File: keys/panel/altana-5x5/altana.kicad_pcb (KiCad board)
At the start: 2 copper layers, 94 x 94 mm, 75 parts, among them SW1 SW_PUSH, SW10 SW_PUSH, SW11 SW_PUSH, SW12 SW_PUSH, SW13 SW_PUSH, SW14 SW_PUSH, SW15 SW_PUSH, SW16 SW_PUSH, SW17 SW_PUSH, SW18 SW_PUSH, SW19 SW_PUSH, SW2 SW_PUSH, SW20 SW_PUSH, SW21 SW_PUSH, SW22 SW_PUSH, SW23 SW_PUSH, SW24 SW_PUSH, SW25 SW_PUSH, SW3 SW_PUSH, SW4 SW_PUSH, SW5 SW_PUSH, SW6 SW_PUSH, SW7 SW_PUSH, SW8 SW_PUSH, SW9 SW_PUSH

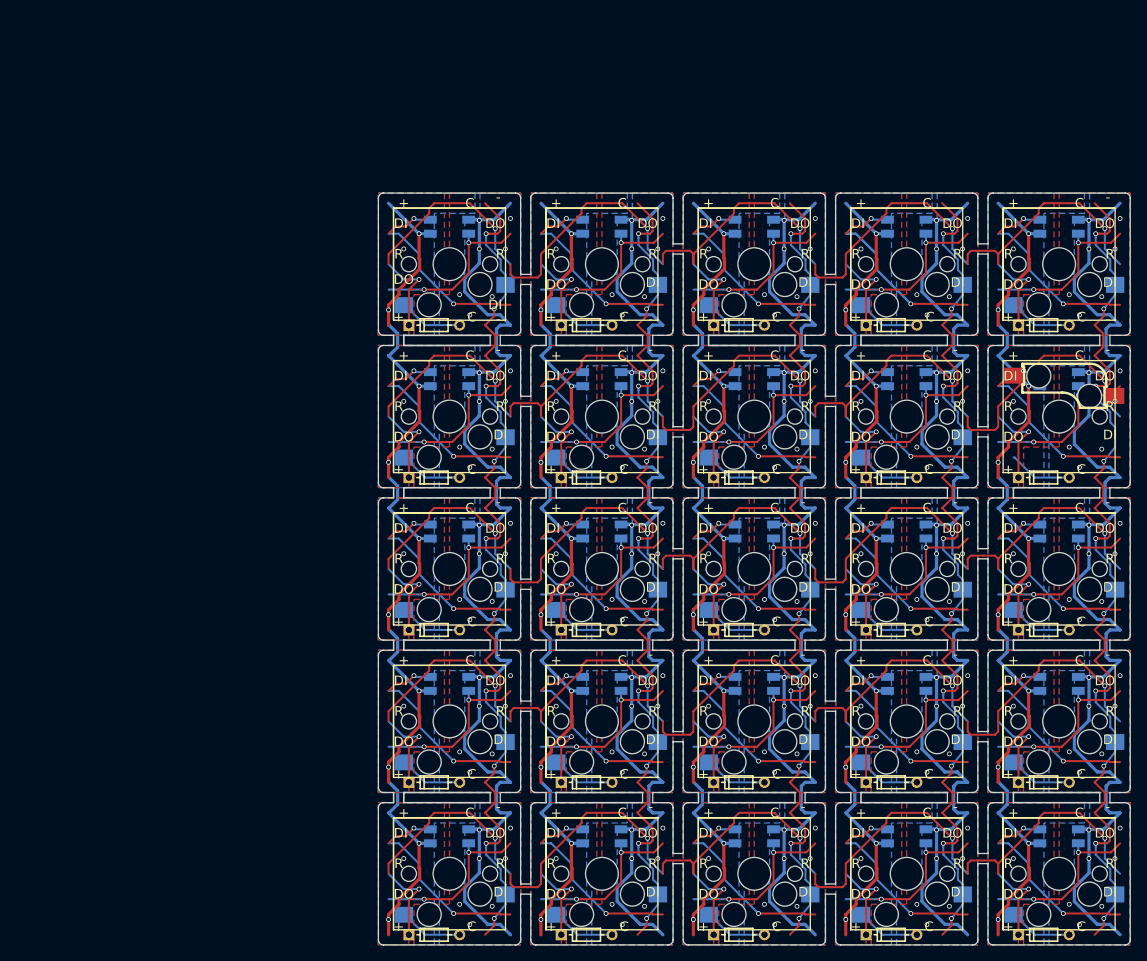
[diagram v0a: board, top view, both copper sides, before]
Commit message: Restore original panel
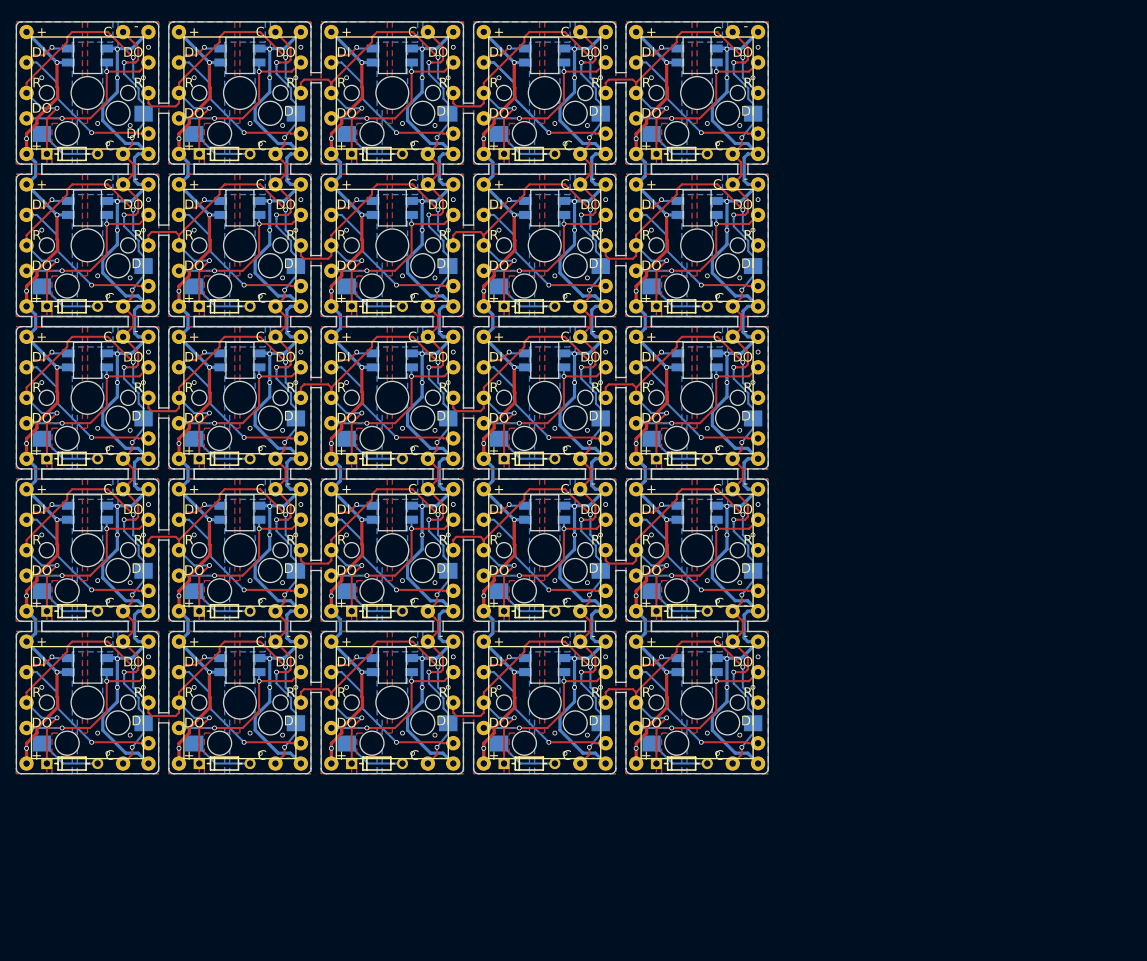
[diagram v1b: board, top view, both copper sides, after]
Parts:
- added REF**: wire pad, footprint:wirepad, B.Cu at (120.1, 54.7)
- added REF**: wire pad, footprint:wirepad, B.Cu at (143.0, 111.9)
- added REF**: wire pad, footprint:wirepad, B.Cu at (158.2, 108.1)
- added REF**: wire pad, footprint:wirepad, B.Cu at (139.2, 108.1)
- added REF**: wire pad, footprint:wirepad, B.Cu at (120.1, 108.1)
- added REF**: wire pad, footprint:wirepad, B.Cu at (101.1, 108.1)
- added REF**: wire pad, footprint:wirepad, B.Cu at (82.0, 108.1)
- added REF**: wire pad, footprint:wirepad, B.Cu at (158.2, 89.0)
- added REF**: wire pad, footprint:wirepad, B.Cu at (139.2, 89.0)
- added REF**: wire pad, footprint:wirepad, B.Cu at (120.1, 89.0)
- added REF**: wire pad, footprint:wirepad, B.Cu at (101.1, 89.0)
- added REF**: wire pad, footprint:wirepad, B.Cu at (82.0, 89.0)
- added REF**: wire pad, footprint:wirepad, B.Cu at (124.0, 111.9)
- added REF**: wire pad, footprint:wirepad, B.Cu at (158.2, 70.0)
- added REF**: wire pad, footprint:wirepad, B.Cu at (139.2, 70.0)
- added REF**: wire pad, footprint:wirepad, B.Cu at (120.1, 70.0)
- added REF**: wire pad, footprint:wirepad, B.Cu at (101.1, 70.0)
- added REF**: wire pad, footprint:wirepad, B.Cu at (82.0, 70.0)
- added REF**: wire pad, footprint:wirepad, B.Cu at (158.2, 50.9)
- added REF**: wire pad, footprint:wirepad, B.Cu at (139.2, 50.9)
- added REF**: wire pad, footprint:wirepad, B.Cu at (120.1, 50.9)
- added REF**: wire pad, footprint:wirepad, B.Cu at (101.1, 50.9)
- added REF**: wire pad, footprint:wirepad, B.Cu at (82.0, 50.9)
- added REF**: wire pad, footprint:wirepad, B.Cu at (104.9, 111.9)
- added REF**: wire pad, footprint:wirepad, B.Cu at (158.2, 31.9)
- added REF**: wire pad, footprint:wirepad, B.Cu at (139.2, 31.9)
- added REF**: wire pad, footprint:wirepad, B.Cu at (120.1, 31.9)
- added REF**: wire pad, footprint:wirepad, B.Cu at (101.1, 31.9)
- added REF**: wire pad, footprint:wirepad, B.Cu at (155.1, 100.5)
- added REF**: wire pad, footprint:wirepad, B.Cu at (143.0, 119.5)
- added REF**: wire pad, footprint:wirepad, B.Cu at (143.0, 104.3)
- added REF**: wire pad, footprint:wirepad, B.Cu at (158.2, 104.3)
- added REF**: wire pad, footprint:wirepad, B.Cu at (155.1, 104.3)
- added REF**: wire pad, footprint:wirepad, B.Cu at (158.2, 119.5)
- added REF**: wire pad, footprint:wirepad, B.Cu at (85.9, 111.9)
- added REF**: wire pad, footprint:wirepad, B.Cu at (155.1, 119.5)
- added REF**: wire pad, footprint:wirepad, B.Cu at (124.0, 119.5)
- added REF**: wire pad, footprint:wirepad, B.Cu at (139.2, 119.5)
- added REF**: wire pad, footprint:wirepad, B.Cu at (136.0, 104.3)
- added REF**: wire pad, footprint:wirepad, B.Cu at (139.2, 104.3)
- added REF**: wire pad, footprint:wirepad, B.Cu at (136.0, 119.5)
- added REF**: wire pad, footprint:wirepad, B.Cu at (124.0, 104.3)
- added REF**: wire pad, footprint:wirepad, B.Cu at (104.9, 104.3)
- added REF**: wire pad, footprint:wirepad, B.Cu at (104.9, 119.5)
- added REF**: wire pad, footprint:wirepad, B.Cu at (120.1, 104.3)
- added REF**: wire pad, footprint:wirepad, B.Cu at (158.2, 92.8)
- added REF**: wire pad, footprint:wirepad, B.Cu at (120.1, 119.5)
- added REF**: wire pad, footprint:wirepad, B.Cu at (117.0, 119.5)
- added REF**: wire pad, footprint:wirepad, B.Cu at (117.0, 104.3)
- added REF**: wire pad, footprint:wirepad, B.Cu at (97.9, 119.5)
- added REF**: wire pad, footprint:wirepad, B.Cu at (101.1, 119.5)
- added REF**: wire pad, footprint:wirepad, B.Cu at (85.9, 104.3)
- added REF**: wire pad, footprint:wirepad, B.Cu at (85.9, 119.5)
- added REF**: wire pad, footprint:wirepad, B.Cu at (101.1, 104.3)
- added REF**: wire pad, footprint:wirepad, B.Cu at (97.9, 104.3)
- added REF**: wire pad, footprint:wirepad, B.Cu at (82.0, 119.5)
- added REF**: wire pad, footprint:wirepad, B.Cu at (139.2, 92.8)
- added REF**: wire pad, footprint:wirepad, B.Cu at (78.9, 119.5)
- added REF**: wire pad, footprint:wirepad, B.Cu at (78.9, 104.3)
- added REF**: wire pad, footprint:wirepad, B.Cu at (66.8, 119.5)
- added REF**: wire pad, footprint:wirepad, B.Cu at (66.8, 104.3)
- added REF**: wire pad, footprint:wirepad, B.Cu at (82.0, 111.9)
- added REF**: wire pad, footprint:wirepad, B.Cu at (66.8, 111.9)
- added REF**: wire pad, footprint:wirepad, B.Cu at (82.0, 104.3)
- added REF**: wire pad, footprint:wirepad, B.Cu at (82.0, 100.5)
- added REF**: wire pad, footprint:wirepad, B.Cu at (66.8, 92.8)
- added REF**: wire pad, footprint:wirepad, B.Cu at (78.9, 85.2)
- added REF**: wire pad, footprint:wirepad, B.Cu at (120.1, 92.8)
- added REF**: wire pad, footprint:wirepad, B.Cu at (82.0, 85.2)
- added REF**: wire pad, footprint:wirepad, B.Cu at (82.0, 92.8)
- added REF**: wire pad, footprint:wirepad, B.Cu at (78.9, 100.5)
- added REF**: wire pad, footprint:wirepad, B.Cu at (66.8, 85.2)
- added REF**: wire pad, footprint:wirepad, B.Cu at (66.8, 100.5)
- added REF**: wire pad, footprint:wirepad, B.Cu at (101.1, 85.2)
- added REF**: wire pad, footprint:wirepad, B.Cu at (85.9, 85.2)
- added REF**: wire pad, footprint:wirepad, B.Cu at (97.9, 85.2)
- added REF**: wire pad, footprint:wirepad, B.Cu at (85.9, 100.5)
- added REF**: wire pad, footprint:wirepad, B.Cu at (97.9, 100.5)
- added REF**: wire pad, footprint:wirepad, B.Cu at (101.1, 92.8)
- added REF**: wire pad, footprint:wirepad, B.Cu at (101.1, 100.5)
- added REF**: wire pad, footprint:wirepad, B.Cu at (117.0, 100.5)
- added REF**: wire pad, footprint:wirepad, B.Cu at (104.9, 85.2)
- added REF**: wire pad, footprint:wirepad, B.Cu at (104.9, 100.5)
- added REF**: wire pad, footprint:wirepad, B.Cu at (117.0, 85.2)
- added REF**: wire pad, footprint:wirepad, B.Cu at (120.1, 85.2)
- added REF**: wire pad, footprint:wirepad, B.Cu at (120.1, 100.5)
- added REF**: wire pad, footprint:wirepad, B.Cu at (124.0, 100.5)
- added REF**: wire pad, footprint:wirepad, B.Cu at (124.0, 85.2)
- added REF**: wire pad, footprint:wirepad, B.Cu at (139.2, 100.5)
- added REF**: wire pad, footprint:wirepad, B.Cu at (143.0, 92.8)
- added REF**: wire pad, footprint:wirepad, B.Cu at (136.0, 85.2)
- added REF**: wire pad, footprint:wirepad, B.Cu at (136.0, 100.5)
- added REF**: wire pad, footprint:wirepad, B.Cu at (139.2, 85.2)
- added REF**: wire pad, footprint:wirepad, B.Cu at (143.0, 100.5)
- added REF**: wire pad, footprint:wirepad, B.Cu at (143.0, 85.2)
- added REF**: wire pad, footprint:wirepad, B.Cu at (158.2, 85.2)
- added REF**: wire pad, footprint:wirepad, B.Cu at (158.2, 100.5)
- added REF**: wire pad, footprint:wirepad, B.Cu at (155.1, 85.2)
- added REF**: wire pad, footprint:wirepad, B.Cu at (155.1, 66.2)
- added REF**: wire pad, footprint:wirepad, B.Cu at (143.0, 66.2)
- added REF**: wire pad, footprint:wirepad, B.Cu at (124.0, 92.8)
- added REF**: wire pad, footprint:wirepad, B.Cu at (158.2, 66.2)
- added REF**: wire pad, footprint:wirepad, B.Cu at (158.2, 81.4)
- added REF**: wire pad, footprint:wirepad, B.Cu at (155.1, 81.4)
- added REF**: wire pad, footprint:wirepad, B.Cu at (143.0, 81.4)
- added REF**: wire pad, footprint:wirepad, B.Cu at (136.0, 81.4)
- added REF**: wire pad, footprint:wirepad, B.Cu at (139.2, 81.4)
- added REF**: wire pad, footprint:wirepad, B.Cu at (124.0, 81.4)
- added REF**: wire pad, footprint:wirepad, B.Cu at (124.0, 66.2)
- added REF**: wire pad, footprint:wirepad, B.Cu at (136.0, 66.2)
- added REF**: wire pad, footprint:wirepad, B.Cu at (139.2, 66.2)
- added REF**: wire pad, footprint:wirepad, B.Cu at (139.2, 73.8)
- added REF**: wire pad, footprint:wirepad, B.Cu at (104.9, 92.8)
- added REF**: wire pad, footprint:wirepad, B.Cu at (120.1, 81.4)
- added REF**: wire pad, footprint:wirepad, B.Cu at (104.9, 81.4)
- added REF**: wire pad, footprint:wirepad, B.Cu at (117.0, 66.2)
- added REF**: wire pad, footprint:wirepad, B.Cu at (104.9, 66.2)
- added REF**: wire pad, footprint:wirepad, B.Cu at (120.1, 66.2)
- added REF**: wire pad, footprint:wirepad, B.Cu at (117.0, 81.4)
- added REF**: wire pad, footprint:wirepad, B.Cu at (85.9, 66.2)
- added REF**: wire pad, footprint:wirepad, B.Cu at (101.1, 81.4)
- added REF**: wire pad, footprint:wirepad, B.Cu at (97.9, 66.2)
- added REF**: wire pad, footprint:wirepad, B.Cu at (97.9, 81.4)
- added REF**: wire pad, footprint:wirepad, B.Cu at (85.9, 92.8)
- added REF**: wire pad, footprint:wirepad, B.Cu at (101.1, 66.2)
- added REF**: wire pad, footprint:wirepad, B.Cu at (85.9, 81.4)
- added REF**: wire pad, footprint:wirepad, B.Cu at (66.8, 81.4)
- added REF**: wire pad, footprint:wirepad, B.Cu at (78.9, 66.2)
- added REF**: wire pad, footprint:wirepad, B.Cu at (82.0, 81.4)
- added REF**: wire pad, footprint:wirepad, B.Cu at (78.9, 81.4)
- added REF**: wire pad, footprint:wirepad, B.Cu at (82.0, 73.8)
- added REF**: wire pad, footprint:wirepad, B.Cu at (82.0, 66.2)
- added REF**: wire pad, footprint:wirepad, B.Cu at (66.8, 66.2)
- added REF**: wire pad, footprint:wirepad, B.Cu at (66.8, 73.8)
- added REF**: wire pad, footprint:wirepad, B.Cu at (143.0, 73.8)
- added REF**: wire pad, footprint:wirepad, B.Cu at (104.9, 62.4)
- added REF**: wire pad, footprint:wirepad, B.Cu at (104.9, 47.1)
- added REF**: wire pad, footprint:wirepad, B.Cu at (104.9, 54.7)
- added REF**: wire pad, footprint:wirepad, B.Cu at (117.0, 62.4)
- added REF**: wire pad, footprint:wirepad, B.Cu at (120.1, 47.1)
- added REF**: wire pad, footprint:wirepad, B.Cu at (120.1, 62.4)
- added REF**: wire pad, footprint:wirepad, B.Cu at (117.0, 47.1)
- added REF**: wire pad, footprint:wirepad, B.Cu at (136.0, 47.1)
- added REF**: wire pad, footprint:wirepad, B.Cu at (124.0, 62.4)
- added REF**: wire pad, footprint:wirepad, B.Cu at (139.2, 54.7)
- added REF**: wire pad, footprint:wirepad, B.Cu at (104.9, 73.8)
- added REF**: wire pad, footprint:wirepad, B.Cu at (139.2, 47.1)
- added REF**: wire pad, footprint:wirepad, B.Cu at (139.2, 62.4)
- added REF**: wire pad, footprint:wirepad, B.Cu at (124.0, 54.7)
- added REF**: wire pad, footprint:wirepad, B.Cu at (136.0, 62.4)
- added REF**: wire pad, footprint:wirepad, B.Cu at (124.0, 47.1)
- added REF**: wire pad, footprint:wirepad, B.Cu at (158.2, 47.1)
- added REF**: wire pad, footprint:wirepad, B.Cu at (158.2, 62.4)
- added REF**: wire pad, footprint:wirepad, B.Cu at (143.0, 54.7)
- added REF**: wire pad, footprint:wirepad, B.Cu at (155.1, 62.4)
- added REF**: wire pad, footprint:wirepad, B.Cu at (155.1, 47.1)
- added REF**: wire pad, footprint:wirepad, B.Cu at (85.9, 73.8)
- added REF**: wire pad, footprint:wirepad, B.Cu at (143.0, 47.1)
- added REF**: wire pad, footprint:wirepad, B.Cu at (143.0, 62.4)
- added REF**: wire pad, footprint:wirepad, B.Cu at (158.2, 54.7)
- added REF**: wire pad, footprint:wirepad, B.Cu at (155.1, 43.3)
- added REF**: wire pad, footprint:wirepad, B.Cu at (155.1, 28.1)
- added REF**: wire pad, footprint:wirepad, B.Cu at (158.2, 28.1)
- added REF**: wire pad, footprint:wirepad, B.Cu at (143.0, 35.7)
- added REF**: wire pad, footprint:wirepad, B.Cu at (143.0, 43.3)
- added REF**: wire pad, footprint:wirepad, B.Cu at (143.0, 28.1)
- added REF**: wire pad, footprint:wirepad, B.Cu at (158.2, 35.7)
- added REF**: wire pad, footprint:wirepad, B.Cu at (158.2, 73.8)
- added REF**: wire pad, footprint:wirepad, B.Cu at (158.2, 43.3)
- added REF**: wire pad, footprint:wirepad, B.Cu at (136.0, 28.1)
- added REF**: wire pad, footprint:wirepad, B.Cu at (139.2, 28.1)
- added REF**: wire pad, footprint:wirepad, B.Cu at (124.0, 35.7)
- added REF**: wire pad, footprint:wirepad, B.Cu at (124.0, 43.3)
- added REF**: wire pad, footprint:wirepad, B.Cu at (124.0, 28.1)
- added REF**: wire pad, footprint:wirepad, B.Cu at (139.2, 35.7)
- added REF**: wire pad, footprint:wirepad, B.Cu at (136.0, 43.3)
- added REF**: wire pad, footprint:wirepad, B.Cu at (139.2, 43.3)
- added REF**: wire pad, footprint:wirepad, B.Cu at (104.9, 35.7)
- added REF**: wire pad, footprint:wirepad, B.Cu at (120.1, 73.8)
- added REF**: wire pad, footprint:wirepad, B.Cu at (104.9, 43.3)
- added REF**: wire pad, footprint:wirepad, B.Cu at (104.9, 28.1)
- added REF**: wire pad, footprint:wirepad, B.Cu at (120.1, 35.7)
- added REF**: wire pad, footprint:wirepad, B.Cu at (117.0, 28.1)
- added REF**: wire pad, footprint:wirepad, B.Cu at (120.1, 43.3)
- added REF**: wire pad, footprint:wirepad, B.Cu at (117.0, 43.3)
- added REF**: wire pad, footprint:wirepad, B.Cu at (120.1, 28.1)
- added REF**: wire pad, footprint:wirepad, B.Cu at (101.1, 62.4)
- added REF**: wire pad, footprint:wirepad, B.Cu at (97.9, 62.4)
- added REF**: wire pad, footprint:wirepad, B.Cu at (85.9, 54.7)
- added REF**: wire pad, footprint:wirepad, B.Cu at (101.1, 73.8)
- added REF**: wire pad, footprint:wirepad, B.Cu at (85.9, 62.4)
- added REF**: wire pad, footprint:wirepad, B.Cu at (85.9, 47.1)
- added REF**: wire pad, footprint:wirepad, B.Cu at (101.1, 54.7)
- added REF**: wire pad, footprint:wirepad, B.Cu at (97.9, 47.1)
- added REF**: wire pad, footprint:wirepad, B.Cu at (101.1, 47.1)
- added REF**: wire pad, footprint:wirepad, B.Cu at (82.0, 62.4)
- added REF**: wire pad, footprint:wirepad, B.Cu at (78.9, 62.4)
- added REF**: wire pad, footprint:wirepad, B.Cu at (66.8, 54.7)
- added REF**: wire pad, footprint:wirepad, B.Cu at (78.9, 47.1)
- added REF**: wire pad, footprint:wirepad, B.Cu at (82.0, 54.7)
- added REF**: wire pad, footprint:wirepad, B.Cu at (158.2, 117.0)
- added REF**: wire pad, footprint:wirepad, B.Cu at (82.0, 47.1)
- added REF**: wire pad, footprint:wirepad, B.Cu at (66.8, 47.1)
- added REF**: wire pad, footprint:wirepad, B.Cu at (66.8, 62.4)
- added REF**: wire pad, footprint:wirepad, B.Cu at (85.9, 35.7)
- added REF**: wire pad, footprint:wirepad, B.Cu at (97.9, 28.1)
- added REF**: wire pad, footprint:wirepad, B.Cu at (85.9, 28.1)
- added REF**: wire pad, footprint:wirepad, B.Cu at (85.9, 43.3)
- added REF**: wire pad, footprint:wirepad, B.Cu at (101.1, 43.3)
- added REF**: wire pad, footprint:wirepad, B.Cu at (101.1, 28.1)
- added REF**: wire pad, footprint:wirepad, B.Cu at (101.1, 35.7)
- added REF**: wire pad, footprint:wirepad, B.Cu at (139.2, 117.0)
- added REF**: wire pad, footprint:wirepad, B.Cu at (97.9, 43.3)
- added REF**: wire pad, footprint:wirepad, B.Cu at (66.8, 38.9)
- added REF**: wire pad, footprint:wirepad, B.Cu at (66.8, 31.9)
- added REF**: wire pad, footprint:wirepad, B.Cu at (82.0, 40.8)
- added REF**: wire pad, footprint:wirepad, B.Cu at (82.0, 31.9)
- added REF**: wire pad, footprint:wirepad, B.Cu at (82.0, 35.7)
- added REF**: wire pad, footprint:wirepad, B.Cu at (66.8, 35.7)
- added REF**: wire pad, footprint:wirepad, B.Cu at (82.0, 28.1)
- added REF**: wire pad, footprint:wirepad, B.Cu at (82.0, 43.3)
- added REF**: wire pad, footprint:wirepad, B.Cu at (66.8, 43.3)
- added REF**: wire pad, footprint:wirepad, B.Cu at (124.0, 73.8)
- added REF**: wire pad, footprint:wirepad, B.Cu at (120.1, 117.0)
- added REF**: wire pad, footprint:wirepad, B.Cu at (66.8, 28.1)
- added REF**: wire pad, footprint:wirepad, B.Cu at (101.1, 117.0)
- added REF**: wire pad, footprint:wirepad, B.Cu at (82.0, 117.0)
- added REF**: wire pad, footprint:wirepad, B.Cu at (158.2, 97.9)
- added REF**: wire pad, footprint:wirepad, B.Cu at (139.2, 97.9)
- added REF**: wire pad, footprint:wirepad, B.Cu at (120.1, 97.9)
- added REF**: wire pad, footprint:wirepad, B.Cu at (101.1, 97.9)
- added REF**: wire pad, footprint:wirepad, B.Cu at (82.0, 97.9)
- added REF**: wire pad, footprint:wirepad, B.Cu at (158.2, 78.9)
- added REF**: wire pad, footprint:wirepad, B.Cu at (139.2, 78.9)
- added REF**: wire pad, footprint:wirepad, B.Cu at (78.9, 43.3)
- added REF**: wire pad, footprint:wirepad, B.Cu at (120.1, 78.9)
- added REF**: wire pad, footprint:wirepad, B.Cu at (101.1, 78.9)
- added REF**: wire pad, footprint:wirepad, B.Cu at (82.0, 78.9)
- added REF**: wire pad, footprint:wirepad, B.Cu at (158.2, 59.8)
- added REF**: wire pad, footprint:wirepad, B.Cu at (139.2, 59.8)
- added REF**: wire pad, footprint:wirepad, B.Cu at (120.1, 59.8)
- added REF**: wire pad, footprint:wirepad, B.Cu at (101.1, 59.8)
- added REF**: wire pad, footprint:wirepad, B.Cu at (82.0, 59.8)
- added REF**: wire pad, footprint:wirepad, B.Cu at (158.2, 40.8)
- added REF**: wire pad, footprint:wirepad, B.Cu at (139.2, 40.8)
- added REF**: wire pad, footprint:wirepad, B.Cu at (78.9, 28.1)
- added REF**: wire pad, footprint:wirepad, B.Cu at (120.1, 40.8)
- added REF**: wire pad, footprint:wirepad, B.Cu at (101.1, 40.8)
- added REF**: wire pad, footprint:wirepad, B.Cu at (143.0, 108.1)
- added REF**: wire pad, footprint:wirepad, B.Cu at (124.0, 108.1)
- added REF**: wire pad, footprint:wirepad, B.Cu at (104.9, 108.1)
- added REF**: wire pad, footprint:wirepad, B.Cu at (85.9, 108.1)
- added REF**: wire pad, footprint:wirepad, B.Cu at (66.8, 108.1)
- added REF**: wire pad, footprint:wirepad, B.Cu at (143.0, 89.0)
- added REF**: wire pad, footprint:wirepad, B.Cu at (124.0, 89.0)
- added REF**: wire pad, footprint:wirepad, B.Cu at (104.9, 89.0)
- added REF**: wire pad, footprint:wirepad, B.Cu at (158.2, 111.9)
- added REF**: wire pad, footprint:wirepad, B.Cu at (85.9, 89.0)
- added REF**: wire pad, footprint:wirepad, B.Cu at (66.8, 89.0)
- added REF**: wire pad, footprint:wirepad, B.Cu at (143.0, 70.0)
- added REF**: wire pad, footprint:wirepad, B.Cu at (124.0, 70.0)
- added REF**: wire pad, footprint:wirepad, B.Cu at (104.9, 70.0)
- added REF**: wire pad, footprint:wirepad, B.Cu at (85.9, 70.0)
- added REF**: wire pad, footprint:wirepad, B.Cu at (66.8, 70.0)
- added REF**: wire pad, footprint:wirepad, B.Cu at (143.0, 50.9)
- added REF**: wire pad, footprint:wirepad, B.Cu at (124.0, 50.9)
- added REF**: wire pad, footprint:wirepad, B.Cu at (104.9, 50.9)
- added REF**: wire pad, footprint:wirepad, B.Cu at (139.2, 111.9)
- added REF**: wire pad, footprint:wirepad, B.Cu at (85.9, 50.9)
- added REF**: wire pad, footprint:wirepad, B.Cu at (66.8, 50.9)
- added REF**: wire pad, footprint:wirepad, B.Cu at (143.0, 31.9)
- added REF**: wire pad, footprint:wirepad, B.Cu at (124.0, 31.9)
- added REF**: wire pad, footprint:wirepad, B.Cu at (104.9, 31.9)
- added REF**: wire pad, footprint:wirepad, B.Cu at (85.9, 31.9)
- added REF**: wire pad, footprint:wirepad, B.Cu at (143.0, 115.1)
- added REF**: wire pad, footprint:wirepad, B.Cu at (124.0, 115.1)
- added REF**: wire pad, footprint:wirepad, B.Cu at (104.9, 115.1)
- added REF**: wire pad, footprint:wirepad, B.Cu at (85.9, 115.1)
- added REF**: wire pad, footprint:wirepad, B.Cu at (120.1, 111.9)
- added REF**: wire pad, footprint:wirepad, B.Cu at (66.8, 115.1)
- added REF**: wire pad, footprint:wirepad, B.Cu at (143.0, 96.0)
- added REF**: wire pad, footprint:wirepad, B.Cu at (124.0, 96.0)
- added REF**: wire pad, footprint:wirepad, B.Cu at (104.9, 96.0)
- added REF**: wire pad, footprint:wirepad, B.Cu at (85.9, 96.0)
- added REF**: wire pad, footprint:wirepad, B.Cu at (66.8, 96.0)
- added REF**: wire pad, footprint:wirepad, B.Cu at (143.0, 77.0)
- added REF**: wire pad, footprint:wirepad, B.Cu at (124.0, 77.0)
- added REF**: wire pad, footprint:wirepad, B.Cu at (104.9, 77.0)
- added REF**: wire pad, footprint:wirepad, B.Cu at (85.9, 77.0)
- added REF**: wire pad, footprint:wirepad, B.Cu at (101.1, 111.9)
- added REF**: wire pad, footprint:wirepad, B.Cu at (66.8, 77.0)
- added REF**: wire pad, footprint:wirepad, B.Cu at (143.0, 57.9)
- added REF**: wire pad, footprint:wirepad, B.Cu at (124.0, 57.9)
- added REF**: wire pad, footprint:wirepad, B.Cu at (104.9, 57.9)
- added REF**: wire pad, footprint:wirepad, B.Cu at (85.9, 57.9)
- added REF**: wire pad, footprint:wirepad, B.Cu at (66.8, 57.9)
- added REF**: wire pad, footprint:wirepad, B.Cu at (143.0, 38.9)
- added REF**: wire pad, footprint:wirepad, B.Cu at (124.0, 38.9)
- added REF**: wire pad, footprint:wirepad, B.Cu at (104.9, 38.9)
- added REF**: wire pad, footprint:wirepad, B.Cu at (85.9, 38.9)
- L1 (x25): moved to F.Cu
- SW1, SW11, SW12, SW13, SW14, SW15, SW16, SW17, SW18, SW19, SW2, SW20, SW21, SW22, SW23, SW24, SW25, SW3, SW4, SW5, SW6, SW7, SW8, SW9: footprint kbd:MX_Hotswap_single -> kbd:CherryMX_Hotswap_single
- SW10: footprint kbd:MX_Hotswap_single -> kbd:CherryMX_Hotswap_single; moved to F.Cu
- moved D 50.1 mm to (107.4, 81.4)
- moved D 50.1 mm to (107.4, 100.5)
- moved D 50.1 mm to (107.4, 43.3)
- moved D 50.1 mm to (107.4, 119.5)
- moved D 50.1 mm to (107.4, 62.4)
- moved L1 50.1 mm to (93.5, 31.0)
- moved L1 50.1 mm to (93.5, 88.2)
- moved L1 50.1 mm to (93.5, 69.1)
- moved L1 50.1 mm to (93.5, 50.1)
- moved L1 50.1 mm to (93.5, 107.2)
- moved SW12 50.1 mm to (93.5, 73.8)
- moved SW17 50.1 mm to (93.5, 92.8)
- moved SW2 50.1 mm to (93.5, 35.7)
- moved SW22 50.1 mm to (93.5, 111.9)
- moved SW7 50.1 mm to (93.5, 54.7)
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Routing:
- net (no net): track 30.8 -> 0.00 mm, vias 1 -> 0
- net /ROW1: track 170.9 -> 201.7 mm, vias 9 -> 10
- net GND: track 749.5 -> 725.4 mm, vias 176 -> 175
- net /ROW0: track 177.6 -> 201.7 mm, vias 9 -> 10
- net Net-(D10-Pad2): track 14.1 -> 8.01 mm, vias 1 -> 0
- net Net-(L1-Pad3): track 659.9 -> 666.0 mm, vias 49 -> 50
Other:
- outline, holes or cut-outs redrawn
